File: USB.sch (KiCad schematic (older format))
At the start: 74 parts, among them J10 10103594-0001LF, Q14 BSS138LT1G, Q18 BSS138LT1G, Q24 BSS138LT1G, Q6 BSS138LT1G, U15 SN74AVC2T245RSWR, U21 M93C46-WMN6TP, U22 TLV62565DBVT, U23 FT4232H-56Q, U24 SN74AVC2T245RSWR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

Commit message: More consistent attributes for LEDs and BSS138
Should match Marble-Mini
Fewer complaints from KiBoM
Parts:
- Q14, Q18, Q24, Q6: HelpURL \\\\cern.ch\\dfs\\Applications\\Altium\\Datasheets\\BSS139.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 -> \\\\cern.ch\\dfs\\Applications\\Altium\\Datasheets\\BSS138L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; Library Name ICs And Semiconductors.DbLib -> ICs And Semiconductors SMD
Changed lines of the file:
@@
 F 1 "BSS138LT1G" H 11369 5605 50  0000 L CNN
 F 2 "ICs And Semiconductors SMD:SOT95P240X110-3N" H 11050 4390 60  0001 L CNN
-F 3 "\\\\cern.ch\\dfs\\Applications\\Altium\\Datasheets\\BSS139.pdf" H 11050 5110 60  0001 L CNN
+F 3 "\\\\cern.ch\\dfs\\Applications\\Altium\\Datasheets\\BSS138LT1G.pdf" H 11050 5110 60  0001 L CNN
 F 4 "BSS138LT1G" H 11050 5020 60  0001 L CNN "Part Number"
 F 5 "N-MOSFET-D 1G 2S 3D" H 11050 4930 60  0001 L CNN "Library Ref"
@@
 F 27 "PcbLib\\ICs And Semiconductors SMD.PcbLib" H 11050 2860 60  0001 L CNN "Footprint Path"
 F 28 "SOT95P240X110-3N" H 11050 2770 60  0001 L CNN "Footprint Ref"
-F 29 "\\\\cern.ch\\dfs\\Applications\\Altium\\Datasheets\\BSS139.pdf" H 11050 2680 60  0001 L CNN "HelpURL"
+F 29 "\\\\cern.ch\\dfs\\Applications\\Altium\\Datasheets\\BSS138LT1G.pdf" H 11050 2680 60  0001 L CNN "HelpURL"
 F 30 "~~" H 11050 2590 60  0001 L CNN "ComponentLink1URL"
 F 31 " " H 11050 2500 60  0001 L CNN "ComponentLink1Description"
@@
 F 35 "03/23/09 00:00:00" H 11050 2140 60  0001 L CNN "CreateDate"
 F 36 "03/23/09 00:00:00" H 11050 2050 60  0001 L CNN "LatestRevisionDate"
-F 37 "ICs And Semiconductors.DbLib" H 11050 1960 60  0001 L CNN "Library Name"
+F 37 "ICs And Semiconductors SMD" H 11050 1960 60  0001 L CNN "Library Name"
 F 38 "This work is licensed under the Creative Commons CC-BY-SA 4.0 License. To the extent that circuit schematics that use Licensed Material can be considered to be ‘Adapted Material’, then the copyright holder waives article 3.b of the license with respect to these schematics." H 11050 1870 60  0001 L CNN "License"
 F 39 "Transistors" H 11050 5600 50  0001 C CNN "Database Table Name"
@@
 F 1 "BSS138LT1G" H 6169 9905 50  0000 L CNN
 F 2 "ICs And Semiconductors SMD:SOT95P240X110-3N" H 5850 8690 60  0001 L CNN
-F 3 "\\\\cern.ch\\dfs\\Applications\\Altium\\Datasheets\\BSS139.pdf" H 5850 9410 60  0001 L CNN
+F 3 "\\\\cern.ch\\dfs\\Applications\\Altium\\Datasheets\\BSS138LT1G.pdf" H 5850 9410 60  0001 L CNN
 F 4 "BSS138LT1G" H 5850 9320 60  0001 L CNN "Part Number"
 F 5 "N-MOSFET-D 1G 2S 3D" H 5850 9230 60  0001 L CNN "Library Ref"
@@
 F 27 "PcbLib\\ICs And Semiconductors SMD.PcbLib" H 5850 7160 60  0001 L CNN "Footprint Path"
 F 28 "SOT95P240X110-3N" H 5850 7070 60  0001 L CNN "Footprint Ref"
-F 29 "\\\\cern.ch\\dfs\\Applications\\Altium\\Datasheets\\BSS139.pdf" H 5850 6980 60  0001 L CNN "HelpURL"
+F 29 "\\\\cern.ch\\dfs\\Applications\\Altium\\Datasheets\\BSS138LT1G.pdf" H 5850 6980 60  0001 L CNN "HelpURL"
 F 30 "~~" H 5850 6890 60  0001 L CNN "ComponentLink1URL"
 F 31 " " H 5850 6800 60  0001 L CNN "ComponentLink1Description"
@@
 F 35 "03/23/09 00:00:00" H 5850 6440 60  0001 L CNN "CreateDate"
 F 36 "03/23/09 00:00:00" H 5850 6350 60  0001 L CNN "LatestRevisionDate"
-F 37 "ICs And Semiconductors.DbLib" H 5850 6260 60  0001 L CNN "Library Name"
+F 37 "ICs And Semiconductors SMD" H 5850 6260 60  0001 L CNN "Library Name"
 F 38 "This work is licensed under the Creative Commons CC-BY-SA 4.0 License. To the extent that circuit schematics that use Licensed Material can be considered to be ‘Adapted Material’, then the copyright holder waives article 3.b of the license with respect to these schematics." H 5850 6170 60  0001 L CNN "License"
 F 39 "Transistors" H 5850 9900 50  0001 C CNN "Database Table Name"
@@
 F 1 "BSS138LT1G" H 5019 10155 50  0000 L CNN
 F 2 "ICs And Semiconductors SMD:SOT95P240X110-3N" H 4700 8940 60  0001 L CNN
-F 3 "\\\\cern.ch\\dfs\\Applications\\Altium\\Datasheets\\BSS139.pdf" H 4700 9660 60  0001 L CNN
+F 3 "\\\\cern.ch\\dfs\\Applications\\Altium\\Datasheets\\BSS138LT1G.pdf" H 4700 9660 60  0001 L CNN
 F 4 "BSS138LT1G" H 4700 9570 60  0001 L CNN "Part Number"
 F 5 "N-MOSFET-D 1G 2S 3D" H 4700 9480 60  0001 L CNN "Library Ref"
@@
 F 27 "PcbLib\\ICs And Semiconductors SMD.PcbLib" H 4700 7410 60  0001 L CNN "Footprint Path"
 F 28 "SOT95P240X110-3N" H 4700 7320 60  0001 L CNN "Footprint Ref"
-F 29 "\\\\cern.ch\\dfs\\Applications\\Altium\\Datasheets\\BSS139.pdf" H 4700 7230 60  0001 L CNN "HelpURL"
+F 29 "\\\\cern.ch\\dfs\\Applications\\Altium\\Datasheets\\BSS138LT1G.pdf" H 4700 7230 60  0001 L CNN "HelpURL"
 F 30 "~~" H 4700 7140 60  0001 L CNN "ComponentLink1URL"
 F 31 " " H 4700 7050 60  0001 L CNN "ComponentLink1Description"
@@
 F 35 "03/23/09 00:00:00" H 4700 6690 60  0001 L CNN "CreateDate"
 F 36 "03/23/09 00:00:00" H 4700 6600 60  0001 L CNN "LatestRevisionDate"
-F 37 "ICs And Semiconductors.DbLib" H 4700 6510 60  0001 L CNN "Library Name"
+F 37 "ICs And Semiconductors SMD" H 4700 6510 60  0001 L CNN "Library Name"
 F 38 "This work is licensed under the Creative Commons CC-BY-SA 4.0 License. To the extent that circuit schematics that use Licensed Material can be considered to be ‘Adapted Material’, then the copyright holder waives article 3.b of the license with respect to these schematics." H 4700 6420 60  0001 L CNN "License"
 F 39 "Transistors" H 4700 10150 50  0001 C CNN "Database Table Name"
@@
 F 1 "BSS138LT1G" H 5019 10555 50  0000 L CNN
 F 2 "ICs And Semiconductors SMD:SOT95P240X110-3N" H 4700 9340 60  0001 L CNN
-F 3 "\\\\cern.ch\\dfs\\Applications\\Altium\\Datasheets\\BSS139.pdf" H 4700 10060 60  0001 L CNN
+F 3 "\\\\cern.ch\\dfs\\Applications\\Altium\\Datasheets\\BSS138LT1G.pdf" H 4700 10060 60  0001 L CNN
 F 4 "BSS138LT1G" H 4700 9970 60  0001 L CNN "Part Number"
 F 5 "N-MOSFET-D 1G 2S 3D" H 4700 9880 60  0001 L CNN "Library Ref"
@@
 F 27 "PcbLib\\ICs And Semiconductors SMD.PcbLib" H 4700 7810 60  0001 L CNN "Footprint Path"
 F 28 "SOT95P240X110-3N" H 4700 7720 60  0001 L CNN "Footprint Ref"
-F 29 "\\\\cern.ch\\dfs\\Applications\\Altium\\Datasheets\\BSS139.pdf" H 4700 7630 60  0001 L CNN "HelpURL"
+F 29 "\\\\cern.ch\\dfs\\Applications\\Altium\\Datasheets\\BSS138LT1G.pdf" H 4700 7630 60  0001 L CNN "HelpURL"
 F 30 "~~" H 4700 7540 60  0001 L CNN "ComponentLink1URL"
 F 31 " " H 4700 7450 60  0001 L CNN "ComponentLink1Description"
@@
 F 35 "03/23/09 00:00:00" H 4700 7090 60  0001 L CNN "CreateDate"
 F 36 "03/23/09 00:00:00" H 4700 7000 60  0001 L CNN "LatestRevisionDate"
-F 37 "ICs And Semiconductors.DbLib" H 4700 6910 60  0001 L CNN "Library Name"
+F 37 "ICs And Semiconductors SMD" H 4700 6910 60  0001 L CNN "Library Name"
 F 38 "This work is licensed under the Creative Commons CC-BY-SA 4.0 License. To the extent that circuit schematics that use Licensed Material can be considered to be ‘Adapted Material’, then the copyright holder waives article 3.b of the license with respect to these schematics." H 4700 6820 60  0001 L CNN "License"
 F 39 "Transistors" H 4700 10550 50  0001 C CNN "Database Table Name"

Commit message: reduced reels with components, DDR 1V5 enable signal connected to MMC, DDR I2C pull-ups powerd from 3.3VP
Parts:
- C162, C167, C168: value CC0603_4.7UF_16V_10%_X5R -> CC0603_4.7UF_25V_10%_X5R; footprint CAPC1709X95N -> Capacitors SMD:CAPC1608X90N; symbol Capacitors_SMD:CC0603_4.7UF_16V_10%_X5R -> Capacitors_SMD:CC0603_4.7UF_25V_10%_X5R; Comment =Value -> 4.7uF; ComponentHeight ~~ -> (none); CreateDate 12/16/13 00:00:00 -> 11/10/14 00:00:00; Database Table Name (none) -> Capacitors SMD; Footprint Library (none) -> Capacitors SMD; Footprint Ref CAPC1709X95N -> CAPC1608X90N; LatestRevisionDate 09/16/14 00:00:00 -> 11/10/14 00:00:00; Library Name Capacitors SMD -> Capacitors.DbLib; Manufacturer Part Number CC0603_4.7UF_16V_10%_X5R -> CC0603_4.7UF_25V_10%_X5R; Manufacturer1 Example TAIYO YUDEN -> MURATA; Manufacturer1 Part Number EMK107ABJ475KA-T -> GRM188R61E475KE11D; PackageDescription ~~ -> (none); Part Number CC0603_4.7UF_16V_10%_X5R -> CC0603_4.7UF_25V_10%_X5R; Pin Count 2.0000000000000000e+00 -> 2; PressFit ~~ -> (none); Sense Comment ~~ -> (none); Status Comment ~~ -> (none); Voltage 16V -> 25V
- C173, C360: footprint CAPC1709X95N -> Capacitors SMD:CAPC1608X90N; symbol Capacitors_SMD:CC0603_4.7UF_16V_10%_X5R -> Capacitors_SMD:CC0603_4.7UF_25V_10%_X5R; Comment =Value -> 4.7uF; ComponentHeight ~~ -> (none); CreateDate 12/16/13 00:00:00 -> 11/10/14 00:00:00; Database Table Name (none) -> Capacitors SMD; Footprint Library (none) -> Capacitors SMD; Footprint Ref CAPC1709X95N -> CAPC1608X90N; LatestRevisionDate 09/16/14 00:00:00 -> 11/10/14 00:00:00; Library Name Capacitors SMD -> Capacitors.DbLib; Manufacturer Part Number CC0603_4.7UF_16V_10%_X5R -> CC0603_4.7UF_25V_10%_X5R; Manufacturer1 Example TAIYO YUDEN -> MURATA; Manufacturer1 Part Number EMK107ABJ475KA-T -> GRM188R61E475KE11D; PackageDescription ~~ -> (none); Part Number CC0603_4.7UF_16V_10%_X5R -> CC0603_4.7UF_25V_10%_X5R; Pin Count 2.0000000000000000e+00 -> 2; PressFit ~~ -> (none); Sense Comment ~~ -> (none); Status Comment ~~ -> (none); Voltage 16V -> 25V

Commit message: Unify CC0603_4.7UF part numbers
C173 C360 update value from library.
Converts them from CC0603_4.7UF_16V_10%_X5R to CC0603_4.7UF_25V_10%_X5R,
matching 18 other instances.
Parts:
- C173, C360: value CC0603_4.7UF_16V_10%_X5R -> CC0603_4.7UF_25V_10%_X5R
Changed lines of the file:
@@
 AR Path="/5C16C03C/5CA532C8" Ref="C173"  Part="1"
 F 0 "C173" V 6000 3350 50  0000 L CNN
-F 1 "CC0603_4.7UF_16V_10%_X5R" H 5900 2990 60  0001 L CNN
+F 1 "CC0603_4.7UF_25V_10%_X5R" H 5900 2990 60  0001 L CNN
 F 2 "Capacitors SMD:CAPC1608X90N" H 5900 2180 60  0001 L CNN
 F 3 "\\\\cern.ch\\dfs\\Applications\\Altium\\Datasheets\\CC0603_X7R_TAIYO-YUDEN_HIGH-VALUE.pdf" H 5900 2810 60  0001 L CNN
@@
 AR Path="/5C16C03C/5D0A6F51" Ref="C360"  Part="1"
 F 0 "C360" V 4900 10650 50  0000 L CNN
-F 1 "CC0603_4.7UF_16V_10%_X5R" H 4800 10290 60  0001 L CNN
+F 1 "CC0603_4.7UF_25V_10%_X5R" H 4800 10290 60  0001 L CNN
 F 2 "Capacitors SMD:CAPC1608X90N" H 4800 9480 60  0001 L CNN
 F 3 "\\\\cern.ch\\dfs\\Applications\\Altium\\Datasheets\\CC0603_X7R_TAIYO-YUDEN_HIGH-VALUE.pdf" H 4800 10110 60  0001 L CNN

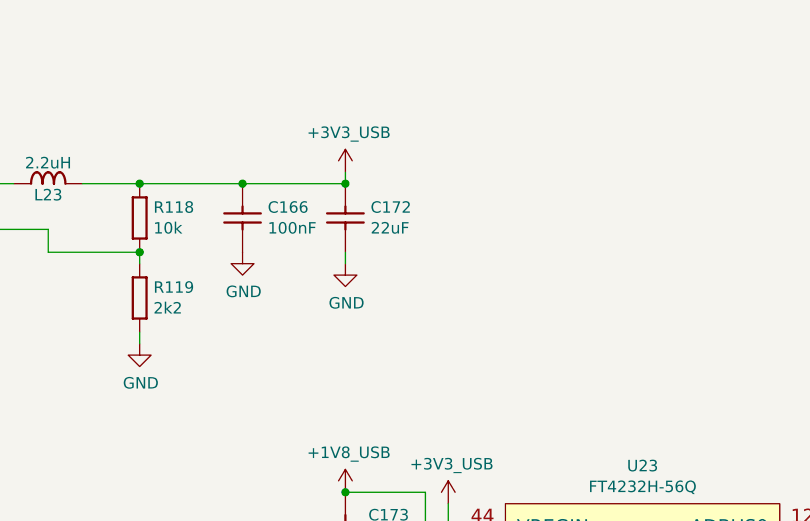
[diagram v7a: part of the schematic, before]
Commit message: fixed drc errors, removed Q25, more test points
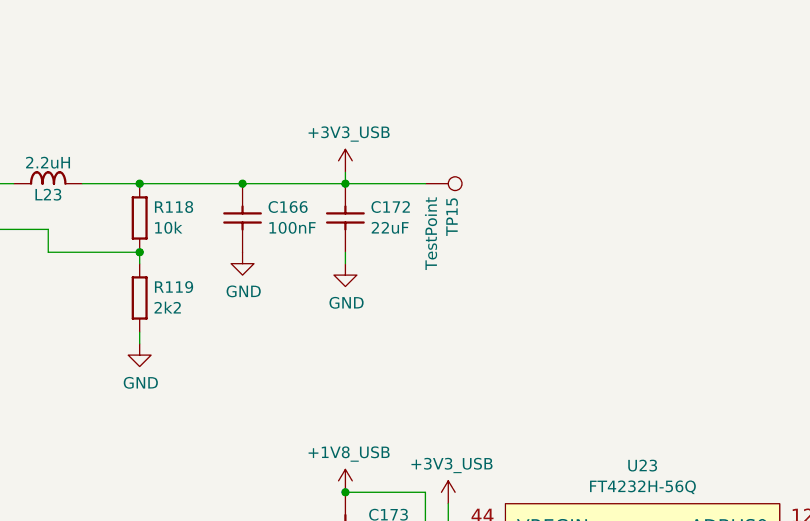
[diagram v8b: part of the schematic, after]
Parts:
- added TP15: TestPoint, TestPoint:TestPoint_THTPad_D1.5mm_Drill0.7mm, symbol Connector_Generic:TestPoint
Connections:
- net +3V3_USB: now also TP15.1
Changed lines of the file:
@@
 NoConn ~ 8000 6300
 NoConn ~ 8000 6500
+$Comp
+L Connector_Generic:TestPoint TP?
+U 1 1 5FCD8B83
+P 6250 1900
+AR Path="/5C16BF8E/5FCD8B83" Ref="TP?"  Part="1"
+AR Path="/5C16BF8E/5DB9B7E6/5FCD8B83" Ref="TP?"  Part="1"
+AR Path="/5C16C03C/5FCD8B83" Ref="TP15"  Part="1"
+F 0 "TP15" H 6308 2018 50  0000 L CNN
+F 1 "TestPoint" H 6308 1927 50  0000 L CNN
+F 2 "TestPoint:TestPoint_THTPad_D1.5mm_Drill0.7mm" H 6450 1900 50  0001 C CNN
+F 3 "~" H 6450 1900 50  0001 C CNN
+	1    6250 1900
+	0    1    1    0
+$EndComp
+Wire Wire Line
+	5900 1900 6250 1900
 $EndSCHEMATC
